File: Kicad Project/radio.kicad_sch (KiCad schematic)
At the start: 103 parts, among them CN20 DF40C-24DP-0.4V, J19 U.FL, J20 U.FL, Q1 MMBT3904-TP, SW3 SW_Push, SW4 SW_Push, U19 TXM27.12M0004322DBBDO00T, U20 CC1101RGPR, U21 0896BM15A0001001E, U22 LC29HBA, U23 EM4095HMSO16B+, U24 PE4259-63, U25 PE4259-63, U26 PE4259-63, U27 PE4259-63, U28 0433BM15A0001001E, U29 PN7160A1HN/C100E, U31 S2B-PH-K-S-GW, U32 S2B-PH-K-S-GW, U33 ESP32-S3-WROOM-1U-N16R2, U34 SiP32508DT, U35 SiP32508DT, U64 TCA9535PWR, U71 SKY13373-460LF, U72 SN74AXC1T45DCKR, Y3 26.0MHz

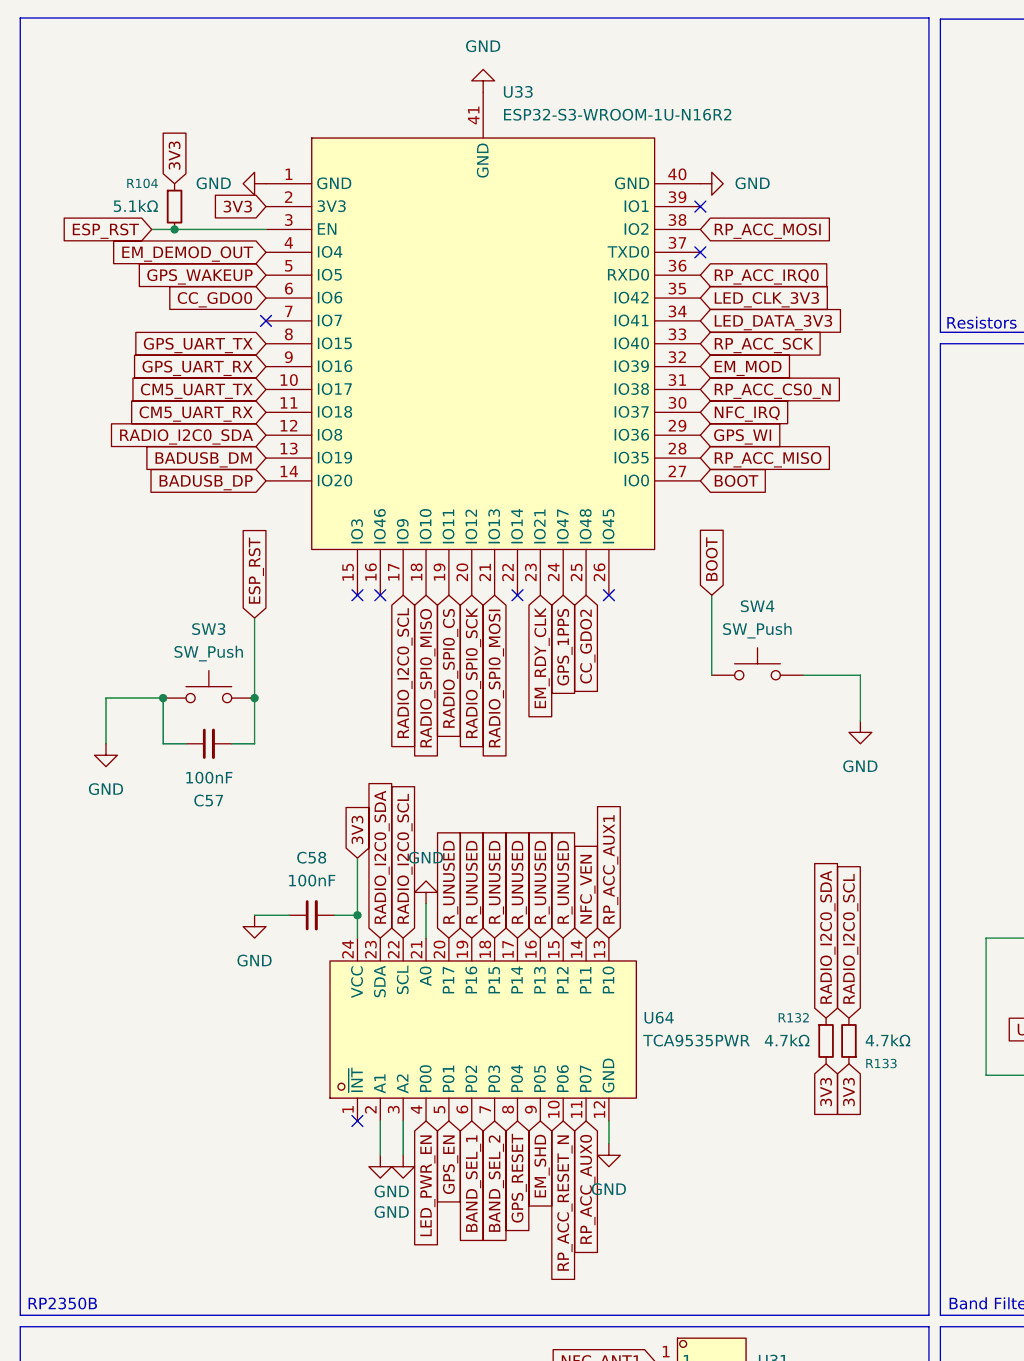
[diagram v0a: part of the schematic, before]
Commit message: organized repo, added license, and readme
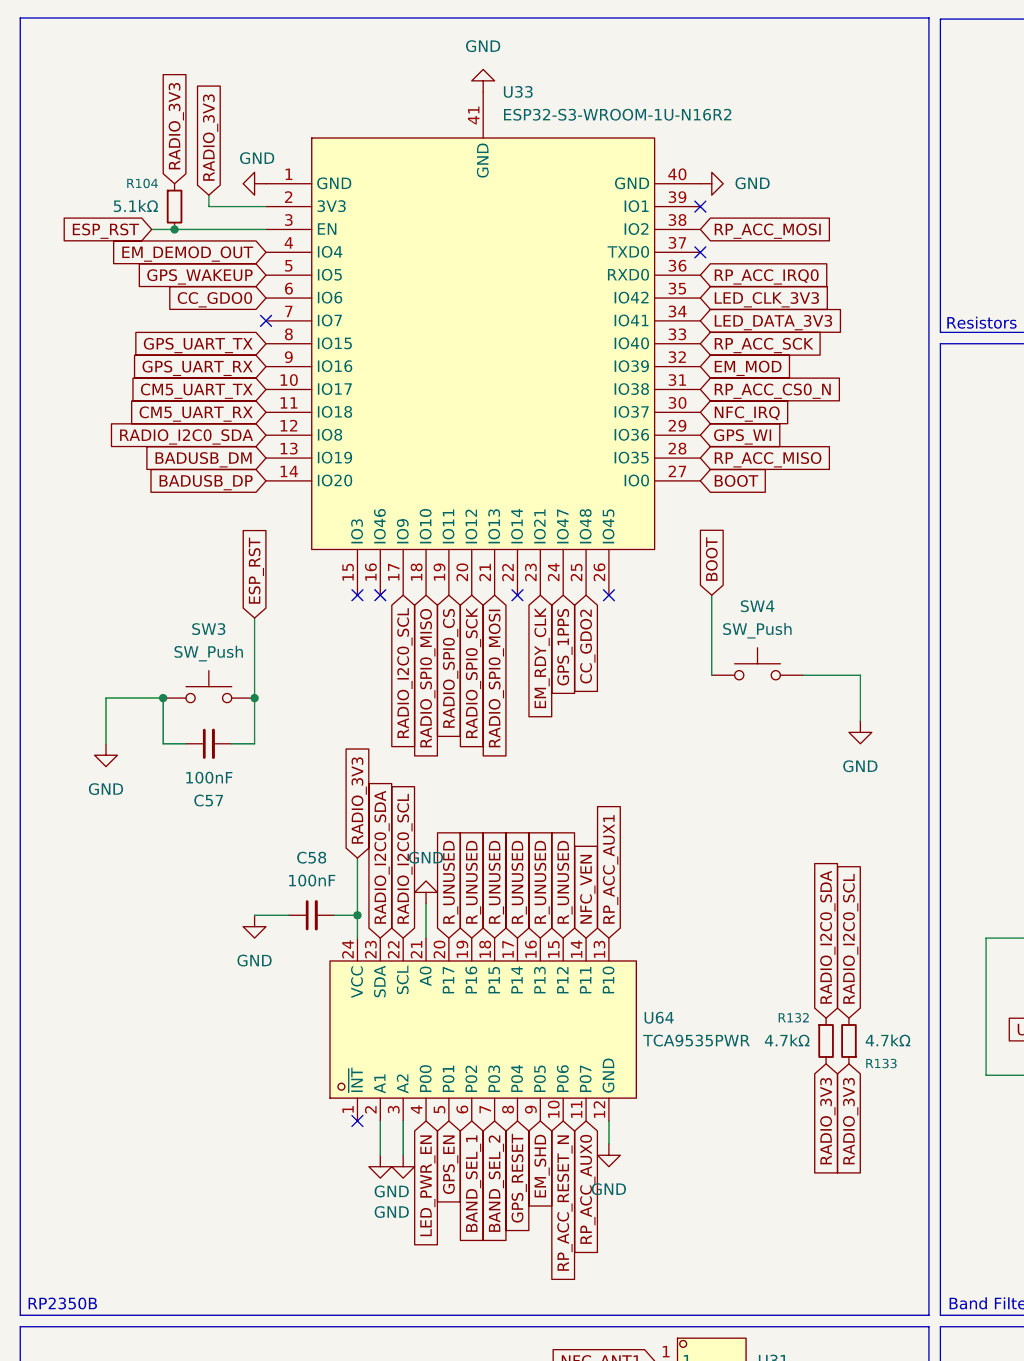
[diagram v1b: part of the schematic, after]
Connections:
- net 3V3: no longer C58.2, R104.1, R132.2, R133.1, U33.2 (3V3), U64.24 (VCC)
- net GPS_VCC: now also C58.2, R104.1, R132.2, R133.1, U33.2 (3V3), U64.24 (VCC)
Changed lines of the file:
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@@
 	(wire
 		(pts
+			(xy 40.64 34.29) (xy 34.29 34.29)
+		)
+		(stroke
+			(width 0)
+			(type default)
+		)
+	)
+	(wire
+		(pts
 			(xy 367.03 190.5) (xy 373.38 190.5)
 		)
@@
 	(wire
 		(pts
+			(xy 34.29 34.29) (xy 34.29 33.02)
+		)
+		(stroke
+			(width 0)
+			(type default)
+		)
+	)
+	(wire
+		(pts
 			(xy 367.03 187.96) (xy 370.84 187.96)
 		)
@@
 		)
 	)
+	(global_label "RADIO_3V3"
+		(shape input)
+		(at 30.48 31.75 90)
+		(fields_autoplaced yes)
+		(effects
+			(font
+				(size 1.27 1.27)
+			)
+			(justify left)
+		)
+		(property "Intersheetrefs" "${INTERSHEET_REFS}"
+			(at 30.48 18.7257 90)
+			(hide yes)
+			(show_name no)
+			(do_not_autoplace no)
+			(effects
+				(font
+					(size 1.27 1.27)
+				)
+				(justify left)
+			)
+		)
+	)
 	(global_label "GPS_VDD_RF"
 		(shape input)
@@
 		)
 	)
-	(global_label "3V3"
-		(shape input)
-		(at 40.64 34.29 180)
-		(fields_autoplaced yes)
-		(effects
-			(font
-				(size 1.27 1.27)
-			)
-			(justify right)
-		)
-		(property "Intersheetrefs" "${INTERSHEET_REFS}"
-			(at 34.1472 34.29 0)
-			(hide yes)
-			(show_name no)
-			(do_not_autoplace no)
-			(effects
-				(font
-					(size 1.27 1.27)
-				)
-				(justify right)
-			)
-		)
-	)
 	(global_label "GND"
 		(shape input)
@@
 		)
 	)
+	(global_label "RADIO_3V3"
+		(shape input)
+		(at 50.8 106.68 90)
+		(fields_autoplaced yes)
+		(effects
+			(font
+				(size 1.27 1.27)
+			)
+			(justify left)
+		)
+		(property "Intersheetrefs" "${INTERSHEET_REFS}"
+			(at 50.8 93.6557 90)
+			(hide yes)
+			(show_name no)
+			(do_not_autoplace no)
+			(effects
+				(font
+					(size 1.27 1.27)
+				)
+				(justify left)
+			)
+		)
+	)
 	(global_label "RADIO_I2C0_SDA"
 		(shape input)
@@
 		)
 	)
+	(global_label "RADIO_3V3"
+		(shape input)
+		(at 105.41 129.54 270)
+		(fields_autoplaced yes)
+		(effects
+			(font
+				(size 1.27 1.27)
+			)
+			(justify right)
+		)
+		(property "Intersheetrefs" "${INTERSHEET_REFS}"
+			(at 105.41 142.5643 90)
+			(hide yes)
+			(show_name no)
+			(do_not_autoplace no)
+			(effects
+				(font
+					(size 1.27 1.27)
+				)
+				(justify right)
+			)
+		)
+	)
 	(global_label "GPS_ANT"
 		(shape input)
@@
 		)
 	)
-	(global_label "3V3"
+	(global_label "RP_ACC_MISO"
 		(shape input)
-		(at 105.41 129.54 270)
+		(at 88.9 62.23 0)
 		(fields_autoplaced yes)
 		(effects
@@
 				(size 1.27 1.27)
 			)
-			(justify right)
+			(justify left)
 		)
 		(property "Intersheetrefs" "${INTERSHEET_REFS}"
-			(at 105.41 136.0328 90)
+			(at 104.5852 62.23 0)
 			(hide yes)
 			(show_name no)
@@
 					(size 1.27 1.27)
 				)
-				(justify right)
+				(justify left)
 			)
 		)
 	)
-	(global_label "RP_ACC_MISO"
+	(global_label "RADIO_3V3"
 		(shape input)
-		(at 88.9 62.23 0)
+		(at 102.87 129.54 270)
 		(fields_autoplaced yes)
 		(effects
@@
 				(size 1.27 1.27)
 			)
-			(justify left)
+			(justify right)
 		)
 		(property "Intersheetrefs" "${INTERSHEET_REFS}"
-			(at 104.5852 62.23 0)
+			(at 102.87 142.5643 90)
 			(hide yes)
 			(show_name no)
@@
 					(size 1.27 1.27)
 				)
-				(justify left)
+				(justify right)
 			)
 		)
@@
 		)
 	)
-	(global_label "3V3"
-		(shape input)
-		(at 50.8 106.68 90)
-		(fields_autoplaced yes)
-		(effects
-			(font
-				(size 1.27 1.27)
-			)
-			(justify left)
-		)
-		(property "Intersheetrefs" "${INTERSHEET_REFS}"
-			(at 50.8 100.1872 90)
-			(hide yes)
-			(show_name no)
-			(do_not_autoplace no)
-			(effects
-				(font
-					(size 1.27 1.27)
-				)
-				(justify left)
-			)
-		)
-	)
 	(global_label "GND"
 		(shape input)
@@
 		)
 	)
-	(global_label "3V3"
-		(shape input)
-		(at 30.48 31.75 90)
-		(fields_autoplaced yes)
-		(effects
-			(font
-				(size 1.27 1.27)
-			)
-			(justify left)
-		)
-		(property "Intersheetrefs" "${INTERSHEET_REFS}"
-			(at 30.48 25.2572 90)
-			(hide yes)
-			(show_name no)
-			(do_not_autoplace no)
-			(effects
-				(font
-					(size 1.27 1.27)
-				)
-				(justify left)
-			)
-		)
-	)
 	(global_label "GND"
 		(shape input)
@@
 		)
 	)
-	(global_label "3V3"
-		(shape input)
-		(at 102.87 129.54 270)
-		(fields_autoplaced yes)
-		(effects
-			(font
-				(size 1.27 1.27)
-			)
-			(justify right)
-		)
-		(property "Intersheetrefs" "${INTERSHEET_REFS}"
-			(at 102.87 136.0328 90)
-			(hide yes)
-			(show_name no)
-			(do_not_autoplace no)
-			(effects
-				(font
-					(size 1.27 1.27)
-				)
-				(justify right)
-			)
-		)
-	)
 	(global_label "GND"
 		(shape input)
@@
 		)
 	)
+	(global_label "RADIO_3V3"
+		(shape input)
+		(at 34.29 33.02 90)
+		(fields_autoplaced yes)
+		(effects
+			(font
+				(size 1.27 1.27)
+			)
+			(justify left)
+		)
+		(property "Intersheetrefs" "${INTERSHEET_REFS}"
+			(at 34.29 19.9957 90)
+			(hide yes)
+			(show_name no)
+			(do_not_autoplace no)
+			(effects
+				(font
+					(size 1.27 1.27)
+				)
+				(justify left)
+			)
+		)
+	)
 	(global_label "GPS_UART_TX"
 		(shape input)
@@
 		(in_pos_files yes)
 		(dnp no)
-		(fields_autoplaced yes)
 		(property "Reference" "#PWR02"
 			(at 34.29 31.75 0)
@@
 		)
 		(property "Value" "GND"
-			(at 36.83 31.7499 90)
+			(at 41.656 28.956 90)
 			(show_name no)
 			(do_not_autoplace no)

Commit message: updated radio schematic, updated slate113 pcb, updated project file
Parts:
- added C? (x2): 10nF, Capacitor_SMD:C_0603_1608Metric, symbol Device:C_Small
- added C? (x3): 220pF, Capacitor_SMD:C_0402_1005Metric, symbol Device:C_Small
- added C?: 100nF, Capacitor_SMD:C_0603_1608Metric, symbol Device:C_Small
- added C?: 1µF, Capacitor_SMD:C_0603_1608Metric, symbol Device:C_Small
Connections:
- net CM5_UART_TX: no longer U72.3 (A)
- net GND: now also C?.1, C?.1, C?.1, C?.1, C?.1, C?.2, C?.2; no longer U20.18 (DGUARD)
- net GPS_UART_RX: now also U33.8 (IO15), U72.3 (A); no longer U33.9 (IO16)
- net GPS_UART_TX: now also U33.9 (IO16); no longer U33.8 (IO15)
- net GPS_VCC: now also C?.1, C?.1
- removed net CC1101_CAPS: U20.11 (AVDD), U20.14 (AVDD), U20.15 (AVDD), U20.9 (AVDD)
- new net: C?.2, U20.18 (DGUARD)
- new net AVDD11_CAP: C?.2, U20.11 (AVDD)
- new net AVDD14_CAP: C?.2, U20.14 (AVDD)
- new net AVDD15_CAP: C?.2, U20.15 (AVDD)
- new net AVDD9_CAP: C?.2, U20.9 (AVDD)
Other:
- moved on the sheet: C25

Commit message: add new journal entry + unsaved radio schematic chnages
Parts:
- gave numbers to parts that had none: 7
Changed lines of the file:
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@@
 		(in_pos_files yes)
 		(dnp no)
-		(property "Reference" "C?"
+		(property "Reference" "C240"
 			(at 274.32 57.15 90)
 			(show_name no)
@@
 			(project "slate113"
 				(path "/5f0cb96f-deec-4f06-b790-14dd96b4fe43"
-					(reference "C?")
+					(reference "C240")
 					(unit 1)
 				)
@@
 		(in_pos_files yes)
 		(dnp no)
-		(property "Reference" "C?"
+		(property "Reference" "C237"
 			(at 248.92 57.15 90)
 			(show_name no)
@@
 			(project "slate113"
 				(path "/5f0cb96f-deec-4f06-b790-14dd96b4fe43"
-					(reference "C?")
+					(reference "C237")
 					(unit 1)
 				)
@@
 		(in_pos_files yes)
 		(dnp no)
-		(property "Reference" "C?"
+		(property "Reference" "C238"
 			(at 248.92 67.31 90)
 			(show_name no)
@@
 			(project "slate113"
 				(path "/5f0cb96f-deec-4f06-b790-14dd96b4fe43"
-					(reference "C?")
+					(reference "C238")
 					(unit 1)
 				)
@@
 		(dnp no)
 		(fields_autoplaced yes)
-		(property "Reference" "C?"
+		(property "Reference" "C236"
 			(at 247.65 118.1162 0)
 			(show_name no)
@@
 			(project "slate113"
 				(path "/5f0cb96f-deec-4f06-b790-14dd96b4fe43"
-					(reference "C?")
+					(reference "C236")
 					(unit 1)
 				)
@@
 		(in_pos_files yes)
 		(dnp no)
-		(property "Reference" "C?"
+		(property "Reference" "C241"
 			(at 294.132 73.914 90)
 			(show_name no)
@@
 			(project "slate113"
 				(path "/5f0cb96f-deec-4f06-b790-14dd96b4fe43"
-					(reference "C?")
+					(reference "C241")
 					(unit 1)
 				)
@@
 		(in_pos_files yes)
 		(dnp no)
-		(property "Reference" "C?"
+		(property "Reference" "C239"
 			(at 251.206 141.478 0)
 			(show_name no)
@@
 			(project "slate113"
 				(path "/5f0cb96f-deec-4f06-b790-14dd96b4fe43"
-					(reference "C?")
+					(reference "C239")
 					(unit 1)
 				)
@@
 		(in_pos_files yes)
 		(dnp no)
-		(property "Reference" "C?"
+		(property "Reference" "C242"
 			(at 300.99 57.15 90)
 			(show_name no)
@@
 			(project "slate113"
 				(path "/5f0cb96f-deec-4f06-b790-14dd96b4fe43"
-					(reference "C?")
+					(reference "C242")
 					(unit 1)
 				)

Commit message: added devlog and worked on NFC stack
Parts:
- added C? (x2): 100nF, Capacitor_SMD:C_0402_1005Metric, symbol Device:C_Small
- added C? (x2): 1nF, Capacitor_SMD:C_0603_1608Metric, symbol Device:C_Small
- added L? (x2): YSPIT0520A-R16M, slate113:IND-SMD_L5.5-W5.3, symbol slate113:YSPIT0520A-R16M
- added R? (x2): 2.7Ω, Resistor_SMD:R_1206_3216Metric, symbol Device:R_Small
- added R? (x2): 2.2kΩ, Capacitor_SMD:C_0603_1608Metric, symbol Device:R_Small
- added R? (x2): 1.5Ω, Resistor_SMD:R_1206_3216Metric, symbol Device:R_Small
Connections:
- net NFC_ANT1: now also R?.2, R?.2
- net NFC_ANT2: now also R?.2, R?.2
- net NFC_RX_N: now also C?.1
- net NFC_RX_P: now also C?.1
- net NFC_TX1: now also R?.1
- net NFC_TX2: now also R?.1
- new net: C?.2, L?.1 (x2)
- new net: L?.2, R?.2 (x2)
- new net: C?.1, R?.1 (x2)
- new net: C?.2, R?.1 (x2)
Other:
- moved on the sheet: CN20, R110, R111, R112, R113, R114, U31

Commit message: wired up NFC, RFID, and GPS systems
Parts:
- removed U32: S2B-PH-K-S-GW, slate113:CONN-TH_S2B-PH-K-S-GW, symbol slate113:S2B-PH-K-S-GW
- added U73: B2B-PH-K-S, slate113:CONN-TH_B2B-PH-K-S, symbol slate113:S2B-PH-K-S-GW
- C35, C66: value 20pF -> 15pF; LCSC Part C1554 -> C26406; MPN 0402CG200J500NT -> CL05C120JB5NNNC
- U19: LCSC Part C20625731 -> C362365; MPN ABM8-272-T3 -> TXM27.12M0004322DBBDO00T; Manufacturer ABRACON -> Yajingxin
- U31: value S2B-PH-K-S-GW -> B2B-PH-K-S; footprint slate113:CONN-TH_S2B-PH-K-S-GW -> slate113:CONN-TH_B2B-PH-K-S; LCSC Part C157932 -> C131337; MPN S2B-PH-K-S-GW -> B2B-PH-K-S(LF)(SN)
- gave numbers to parts that had none: 12
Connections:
- net 3V3: no longer C88.1, C91.1, C92.1, D4.2 (A), U22.22 (V_BCKP)
- net RFID_ANT1: now also U73.1
- net RFID_ANT2: now also U73.2
- net GPS_VCC renamed GPS_VBCKP
- net GPS_VBCKP: now also C88.1, C91.1, C92.1, D4.2 (A), U22.22 (V_BCKP)

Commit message: finish up radio daughter board
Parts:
- removed R111: 10kΩ, Resistor_SMD:R_0603_1608Metric, symbol Device:R_Small
- added FB11: FerriteBead, Inductor_SMD:L_0603_1608Metric, symbol Device:FerriteBead
- added R153: 10kΩ, Resistor_SMD:R_0603_1608Metric, symbol Device:R_Small
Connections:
- net FerriteGND_Carrier is gone; now on net FerriteGND_RADIO: CN20.25, CN20.26, CN20.27, CN20.28
- net GPS_EN is gone; now on net R_UNUSED: U64.5 (P01)
- net FerriteGND_RADIO: now also FB11.1
- net GND: now also FB11.2, R153.1
- net R_UNUSED: now also R153.2
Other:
- moved on the sheet: R115, R116, R117, R118, R119, R120
